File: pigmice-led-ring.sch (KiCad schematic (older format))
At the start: 27 parts, among them J1 Conn_01x02_Female, J2 Conn_01x03_Female

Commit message: WIP v0.3.0 work
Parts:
- removed D1, D10, D11, D12, D13, D14, D15, D16, D17, D18, D19, D2, D20, D21, D22, D23, D24, D3, D4, D5, D6, D7, D8, D9: LED, LED_SMD:LED_Avago_PLCC4_3.2x2.8mm_CW, symbol Device:LED
- removed PS1: RCD-24-0.35_Vref, CONV_RCD-24-0:Vref, symbol RCD-24-0.35_Vref:RCD-24-0.35_Vref
- added C1: 2.2uF, Capacitor_SMD:C_0805_2012Metric, symbol Device:C
- added C2: 4.7uF, Capacitor_SMD:C_0805_2012Metric, symbol Device:C
- added CF1: 330pF, Capacitor_SMD:C_0805_2012Metric, symbol Device:C
- added D1: D_Schottky, Diode_SMD:D_SOD-123, symbol Device:D_Schottky
- added D10, D11, D12, D13, D14, D15, D16, D17, D18, D19, D2, D20, D21, D22, D23, D24, D25, D26, D3, D4, D5, D6, D7, D8, D9: LED, led-ring:LED_Avago_PLCC4_3.2x2.8mm_CW, symbol Device:LED_Small
- added L1: 10uH, Inductor_SMD:L_Taiyo-Yuden_NR-40xx, symbol Device:L
- added R1: 203k, Resistor_SMD:R_0805_2012Metric, symbol Device:R
- added R2: 13.3k, Resistor_SMD:R_0805_2012Metric, symbol Device:R
- added R3: 47k, Resistor_SMD:R_0805_2012Metric, symbol Device:R_Small
- added R4, R5, R6, R7, R8: 150Ω, Resistor_SMD:R_0805_2012Metric, symbol Device:R_Small
- added U1: LMR62014XMF, Package_TO_SOT_SMD:SOT-23-5, symbol Regulator_Switching:LMR62014XMF
- J1: footprint led-ring:45A-VERT-PAIR -> Connector_Wire:SolderWirePad_1x02_P3.81mm_Drill1mm
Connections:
- net labels added: Vbat, Vled
- net labels removed: NULL, VCC
- wire segments 61 -> 59
- no-connect marks 2 -> 1
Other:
- note added: "20V output"

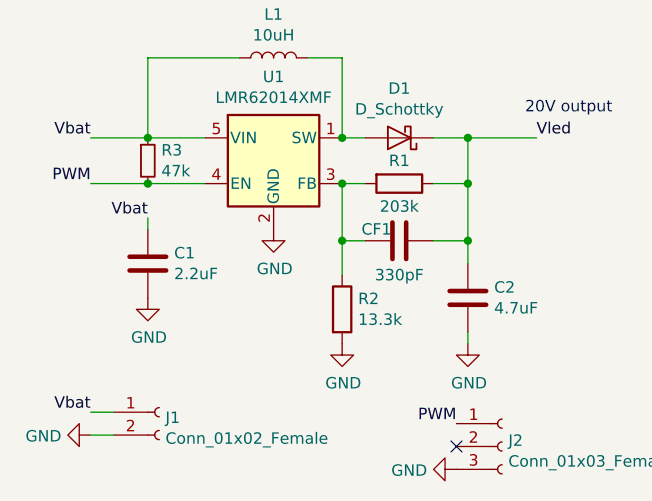
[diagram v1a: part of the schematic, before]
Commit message: Fix R2/CF1 labels
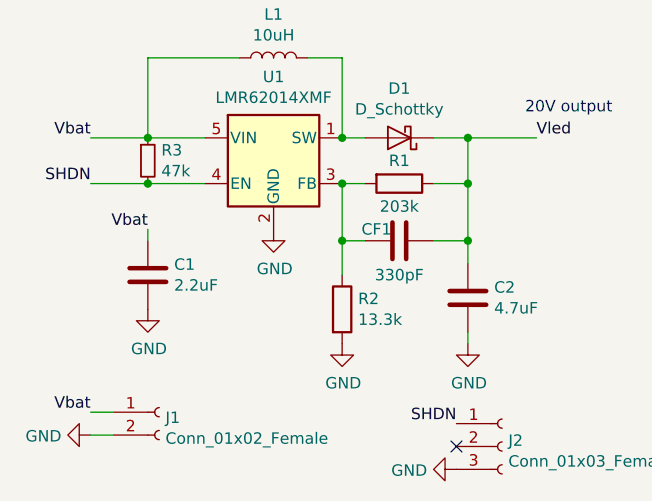
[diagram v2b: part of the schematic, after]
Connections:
- net PWM renamed SHDN
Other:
- moved on the sheet: C1
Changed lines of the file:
@@
 Vbat
 Text Label 1650 3450 2    50   ~ 0
-PWM
+SHDN
 $Comp
 L Device:D_Schottky D1
@@
 	0    -1   -1   0
 $EndComp
-$Comp
-L Device:C C2
-U 1 1 5E1D29D8
-P 3300 3950
-F 0 "C2" H 3415 3996 50  0000 L CNN
-F 1 "4.7uF" H 3415 3905 50  0000 L CNN
-F 2 "Capacitor_SMD:C_0805_2012Metric" H 3338 3800 50  0001 C CNN
-F 3 "~" H 3300 3950 50  0001 C CNN
-	1    3300 3950
-	1    0    0    -1
-$EndComp
 Text Label 3600 3250 0    50   ~ 0
 Vled
@@
 Connection ~ 2750 3700
 Wire Wire Line
-	3300 4150 3300 4100
-Wire Wire Line
 	3150 3700 3300 3700
 Wire Wire Line
-	3300 3700 3300 3800
-Wire Wire Line
 	3150 3450 3300 3450
 Wire Wire Line
 	3300 3450 3300 3700
-Connection ~ 3300 3700
 Wire Wire Line
 	3150 3250 3300 3250
@@
 $EndComp
 Text Label 3250 4500 2    50   ~ 0
-PWM
+SHDN
 NoConn ~ 3250 4600
 Wire Wire Line
@@
 	1650 3250 1900 3250
 Connection ~ 1900 3250
-Wire Wire Line
-	2150 3250 1900 3250
 Wire Wire Line
 	1900 2900 1900 3250
@@
 	4700 4500 4550 4500
 Connection ~ 4700 4500
-Wire Wire Line
-	1650 3450 1900 3450
-Text Label 1900 3600 2    50   ~ 0
+Text Label 1900 3650 2    50   ~ 0
 Vbat
 Wire Wire Line
-	1900 3600 1900 3650
+	1900 3650 1900 3700
 $Comp
 L Device:C C1
 U 1 1 5E1D1330
-P 1900 3800
-F 0 "C1" H 2015 3846 50  0000 L CNN
-F 1 "2.2uF" H 2015 3755 50  0000 L CNN
-F 2 "Capacitor_SMD:C_0805_2012Metric" H 1938 3650 50  0001 C CNN
-F 3 "~" H 1900 3800 50  0001 C CNN
-	1    1900 3800
+P 1900 3850
+F 0 "C1" H 2015 3896 50  0000 L CNN
+F 1 "2.2uF" H 2015 3805 50  0000 L CNN
+F 2 "Capacitor_SMD:C_0805_2012Metric" H 1938 3700 50  0001 C CNN
+F 3 "~" H 1900 3850 50  0001 C CNN
+	1    1900 3850
 	1    0    0    -1
 $EndComp
@@
 L power:GND #PWR0101
 U 1 1 5E24B903
-P 1900 3950
-F 0 "#PWR0101" H 1900 3700 50  0001 C CNN
-F 1 "GND" H 1905 3777 50  0000 C CNN
-F 2 "" H 1900 3950 50  0001 C CNN
-F 3 "" H 1900 3950 50  0001 C CNN
-	1    1900 3950
+P 1900 4000
+F 0 "#PWR0101" H 1900 3750 50  0001 C CNN
+F 1 "GND" H 1905 3827 50  0000 C CNN
+F 2 "" H 1900 4000 50  0001 C CNN
+F 3 "" H 1900 4000 50  0001 C CNN
+	1    1900 4000
 	1    0    0    -1
 $EndComp
@@
 $EndComp
 $Comp
+L Device:R_Small R8
+U 1 1 5E1D7BE7
+P 5900 3150
+F 0 "R8" H 5959 3196 50  0000 L CNN
+F 1 "150Ω" H 5959 3105 50  0000 L CNN
+F 2 "Resistor_SMD:R_0805_2012Metric" H 5900 3150 50  0001 C CNN
+F 3 "~" H 5900 3150 50  0001 C CNN
+	1    5900 3150
+	1    0    0    -1
+$EndComp
+$Comp
+L Device:LED_Small D22
+U 1 1 5E1D7BEE
+P 5900 3400
+F 0 "D22" V 5946 3332 50  0000 R CNN
+F 1 "LED" V 5855 3332 50  0000 R CNN
+F 2 "led-ring:LED_Avago_PLCC4_3.2x2.8mm_CW" V 5900 3400 50  0001 C CNN
+F 3 "~" V 5900 3400 50  0001 C CNN
+	1    5900 3400
+	0    -1   -1   0
+$EndComp
+$Comp
+L Device:LED_Small D23
+U 1 1 5E1D7BF5
+P 5900 3650
+F 0 "D23" V 5946 3582 50  0000 R CNN
+F 1 "LED" V 5855 3582 50  0000 R CNN
+F 2 "led-ring:LED_Avago_PLCC4_3.2x2.8mm_CW" V 5900 3650 50  0001 C CNN
+F 3 "~" V 5900 3650 50  0001 C CNN
+	1    5900 3650
+	0    -1   -1   0
+$EndComp
+$Comp
+L Device:LED_Small D24
+U 1 1 5E1D7BFC
+P 5900 3900
+F 0 "D24" V 5946 3832 50  0000 R CNN
+F 1 "LED" V 5855 3832 50  0000 R CNN
+F 2 "led-ring:LED_Avago_PLCC4_3.2x2.8mm_CW" V 5900 3900 50  0001 C CNN
+F 3 "~" V 5900 3900 50  0001 C CNN
+	1    5900 3900
+	0    -1   -1   0
+$EndComp
+$Comp
+L Device:LED_Small D25
+U 1 1 5E1D7C03
+P 5900 4150
+F 0 "D25" V 5946 4082 50  0000 R CNN
+F 1 "LED" V 5855 4082 50  0000 R CNN
+F 2 "led-ring:LED_Avago_PLCC4_3.2x2.8mm_CW" V 5900 4150 50  0001 C CNN
+F 3 "~" V 5900 4150 50  0001 C CNN
+	1    5900 4150
+	0    -1   -1   0
+$EndComp
+$Comp
+L Device:LED_Small D26
+U 1 1 5E1D7C0A
+P 5900 4400
+F 0 "D26" V 5946 4332 50  0000 R CNN
+F 1 "LED" V 5855 4332 50  0000 R CNN
+F 2 "led-ring:LED_Avago_PLCC4_3.2x2.8mm_CW" V 5900 4400 50  0001 C CNN
+F 3 "~" V 5900 4400 50  0001 C CNN
+	1    5900 4400
+	0    -1   -1   0
+$EndComp
+Wire Wire Line
+	5900 3250 5900 3300
+Wire Wire Line
+	5900 3550 5900 3500
+Wire Wire Line
+	5900 3750 5900 3800
+Wire Wire Line
+	5900 4000 5900 4050
+Wire Wire Line
+	5900 4250 5900 4300
+Wire Wire Line
+	5600 3050 5900 3050
+Connection ~ 5600 3050
+Wire Wire Line
+	5900 4500 5600 4500
+Connection ~ 5600 4500
+Connection ~ 3300 3700
+Wire Wire Line
+	3300 3700 3300 3800
+$Comp
 L power:GND #PWR0107
 U 1 1 5E254103
@@
 	1    0    0    -1
 $EndComp
+Wire Wire Line
+	3300 4150 3300 4100
+$Comp
+L Device:C C2
+U 1 1 5E1D29D8
+P 3300 3950
+F 0 "C2" H 3415 3996 50  0000 L CNN
+F 1 "4.7uF" H 3415 3905 50  0000 L CNN
+F 2 "Capacitor_SMD:C_0805_2012Metric" H 3338 3800 50  0001 C CNN
+F 3 "~" H 3300 3950 50  0001 C CNN
+	1    3300 3950
+	1    0    0    -1
+$EndComp
+Connection ~ 1900 3450
+Wire Wire Line
+	1650 3450 1900 3450
+Wire Wire Line
+	1900 3450 2150 3450
+Wire Wire Line
+	2150 3250 1900 3250
 $Comp
 L Device:R_Small R3
@@
 	1    0    0    -1
 $EndComp
-Connection ~ 1900 3450
-Wire Wire Line
-	1900 3450 2150 3450
-$Comp
-L Device:R_Small R8
-U 1 1 5E1D7BE7
-P 5900 3150
-F 0 "R8" H 5959 3196 50  0000 L CNN
-F 1 "150Ω" H 5959 3105 50  0000 L CNN
-F 2 "Resistor_SMD:R_0805_2012Metric" H 5900 3150 50  0001 C CNN
-F 3 "~" H 5900 3150 50  0001 C CNN
-	1    5900 3150
-	1    0    0    -1
-$EndComp
-$Comp
-L Device:LED_Small D22
-U 1 1 5E1D7BEE
-P 5900 3400
-F 0 "D22" V 5946 3332 50  0000 R CNN
-F 1 "LED" V 5855 3332 50  0000 R CNN
-F 2 "led-ring:LED_Avago_PLCC4_3.2x2.8mm_CW" V 5900 3400 50  0001 C CNN
-F 3 "~" V 5900 3400 50  0001 C CNN
-	1    5900 3400
-	0    -1   -1   0
-$EndComp
-$Comp
-L Device:LED_Small D23
-U 1 1 5E1D7BF5
-P 5900 3650
-F 0 "D23" V 5946 3582 50  0000 R CNN
-F 1 "LED" V 5855 3582 50  0000 R CNN
-F 2 "led-ring:LED_Avago_PLCC4_3.2x2.8mm_CW" V 5900 3650 50  0001 C CNN
-F 3 "~" V 5900 3650 50  0001 C CNN
-	1    5900 3650
-	0    -1   -1   0
-$EndComp
-$Comp
-L Device:LED_Small D24
-U 1 1 5E1D7BFC
-P 5900 3900
-F 0 "D24" V 5946 3832 50  0000 R CNN
-F 1 "LED" V 5855 3832 50  0000 R CNN
-F 2 "led-ring:LED_Avago_PLCC4_3.2x2.8mm_CW" V 5900 3900 50  0001 C CNN
-F 3 "~" V 5900 3900 50  0001 C CNN
-	1    5900 3900
-	0    -1   -1   0
-$EndComp
-$Comp
-L Device:LED_Small D25
-U 1 1 5E1D7C03
-P 5900 4150
-F 0 "D25" V 5946 4082 50  0000 R CNN
-F 1 "LED" V 5855 4082 50  0000 R CNN
-F 2 "led-ring:LED_Avago_PLCC4_3.2x2.8mm_CW" V 5900 4150 50  0001 C CNN
-F 3 "~" V 5900 4150 50  0001 C CNN
-	1    5900 4150
-	0    -1   -1   0
-$EndComp
-$Comp
-L Device:LED_Small D26
-U 1 1 5E1D7C0A
-P 5900 4400
-F 0 "D26" V 5946 4332 50  0000 R CNN
-F 1 "LED" V 5855 4332 50  0000 R CNN
-F 2 "led-ring:LED_Avago_PLCC4_3.2x2.8mm_CW" V 5900 4400 50  0001 C CNN
-F 3 "~" V 5900 4400 50  0001 C CNN
-	1    5900 4400
-	0    -1   -1   0
-$EndComp
-Wire Wire Line
-	5900 3250 5900 3300
-Wire Wire Line
-	5900 3550 5900 3500
-Wire Wire Line
-	5900 3750 5900 3800
-Wire Wire Line
-	5900 4000 5900 4050
-Wire Wire Line
-	5900 4250 5900 4300
-Wire Wire Line
-	5600 3050 5900 3050
-Connection ~ 5600 3050
-Wire Wire Line
-	5900 4500 5600 4500
-Connection ~ 5600 4500
 $EndSCHEMATC

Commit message: Swap out inductor for smaller 2410 footprint
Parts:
- L1: footprint Inductor_SMD:L_Taiyo-Yuden_NR-40xx -> Inductor_SMD:L_Taiyo-Yuden_NR-24xx
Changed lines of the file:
@@
 F 0 "L1" V 2640 2900 50  0000 C CNN
 F 1 "10uH" V 2549 2900 50  0000 C CNN
-F 2 "Inductor_SMD:L_Taiyo-Yuden_NR-40xx" H 2450 2900 50  0001 C CNN
+F 2 "Inductor_SMD:L_Taiyo-Yuden_NR-24xx" H 2450 2900 50  0001 C CNN
 F 3 "~" H 2450 2900 50  0001 C CNN
 	1    2450 2900

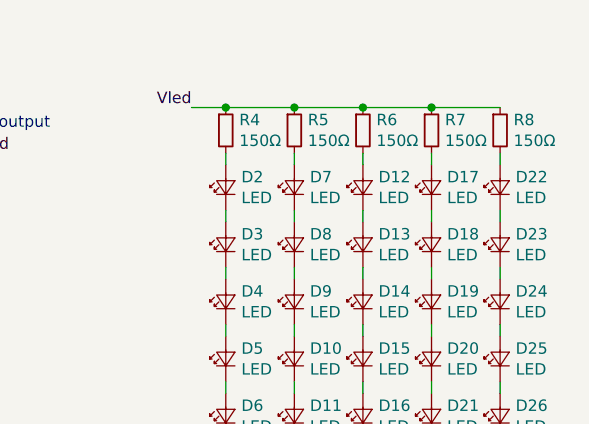
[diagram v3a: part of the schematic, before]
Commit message: Switch from 150 to 137 ohm resistors for LEDs
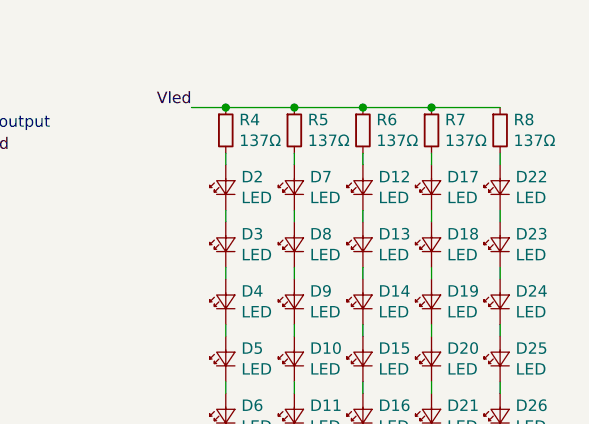
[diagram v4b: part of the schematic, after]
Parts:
- R4, R5, R6, R7, R8: value 150Ω -> 137Ω
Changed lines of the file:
@@
 P 4700 3150
 F 0 "R4" H 4759 3196 50  0000 L CNN
-F 1 "150Ω" H 4759 3105 50  0000 L CNN
+F 1 "137Ω" H 4759 3105 50  0000 L CNN
 F 2 "Resistor_SMD:R_0805_2012Metric" H 4700 3150 50  0001 C CNN
 F 3 "~" H 4700 3150 50  0001 C CNN
@@
 P 5000 3150
 F 0 "R5" H 5059 3196 50  0000 L CNN
-F 1 "150Ω" H 5059 3105 50  0000 L CNN
+F 1 "137Ω" H 5059 3105 50  0000 L CNN
 F 2 "Resistor_SMD:R_0805_2012Metric" H 5000 3150 50  0001 C CNN
 F 3 "~" H 5000 3150 50  0001 C CNN
@@
 P 5300 3150
 F 0 "R6" H 5359 3196 50  0000 L CNN
-F 1 "150Ω" H 5359 3105 50  0000 L CNN
+F 1 "137Ω" H 5359 3105 50  0000 L CNN
 F 2 "Resistor_SMD:R_0805_2012Metric" H 5300 3150 50  0001 C CNN
 F 3 "~" H 5300 3150 50  0001 C CNN
@@
 P 5600 3150
 F 0 "R7" H 5659 3196 50  0000 L CNN
-F 1 "150Ω" H 5659 3105 50  0000 L CNN
+F 1 "137Ω" H 5659 3105 50  0000 L CNN
 F 2 "Resistor_SMD:R_0805_2012Metric" H 5600 3150 50  0001 C CNN
 F 3 "~" H 5600 3150 50  0001 C CNN
@@
 P 5900 3150
 F 0 "R8" H 5959 3196 50  0000 L CNN
-F 1 "150Ω" H 5959 3105 50  0000 L CNN
+F 1 "137Ω" H 5959 3105 50  0000 L CNN
 F 2 "Resistor_SMD:R_0805_2012Metric" H 5900 3150 50  0001 C CNN
 F 3 "~" H 5900 3150 50  0001 C CNN

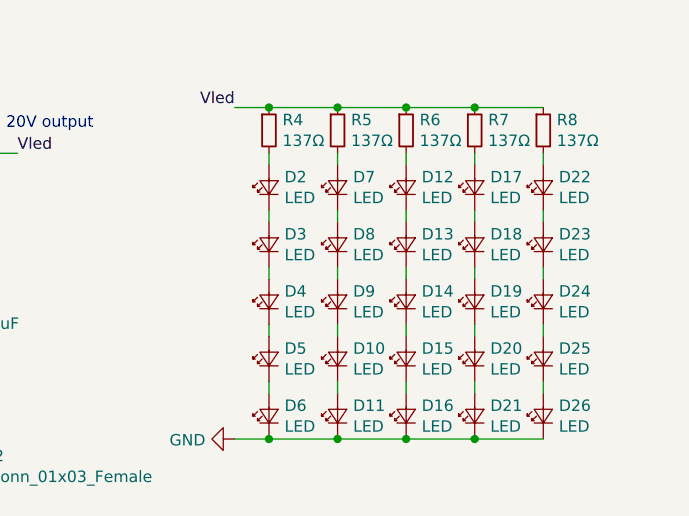
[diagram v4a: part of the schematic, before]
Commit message: Use CCRs instead of resistors
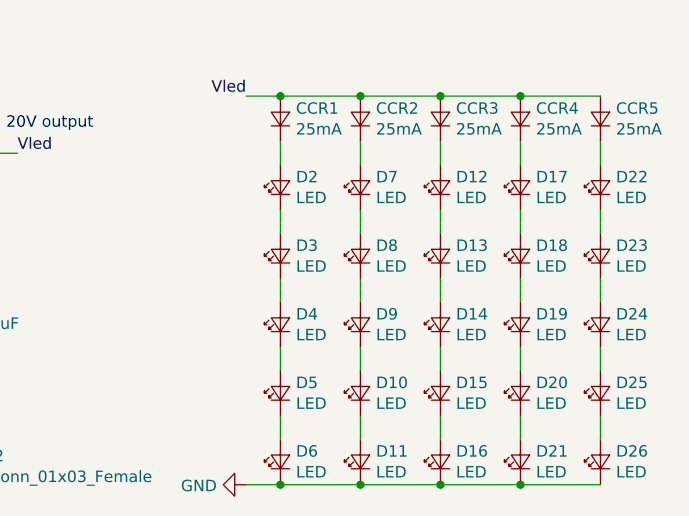
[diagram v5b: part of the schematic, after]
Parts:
- removed R4, R5, R6, R7, R8: 137Ω, Resistor_SMD:R_0805_2012Metric, symbol Device:R_Small
- added CCR1, CCR2, CCR3, CCR4, CCR5: 25mA, Diode_SMD:D_SOD-123, symbol Device:D_Small
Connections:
- net Vled: now also CCR1.2 (A), CCR2.2 (A), CCR3.2 (A), CCR4.2 (A), CCR5.2 (A)
- net at D22.2 (A): now also CCR5.1 (K)
- net at D2.2 (A): now also CCR1.1 (K)
- net at D7.2 (A): now also CCR2.1 (K)
- net at D12.2 (A): now also CCR3.1 (K)
- net at D17.2 (A): now also CCR4.1 (K)

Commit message: Add mini badge
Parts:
- added BT1: Battery_Cell, Battery:BatteryHolder_LINX_BAT-HLD-012-SMT, symbol Device:Battery_Cell
- added D27, D28, D29, D30: LED, LED_SMD:LED_0603_1608Metric, symbol Device:LED
- added R4, R5: 47Ω, Resistor_SMD:R_0603_1608Metric, symbol Device:R
- added R6, R7: 56Ω, Resistor_SMD:R_0603_1608Metric, symbol Device:R
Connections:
- new net: BT1.1 (+), R4.1, R5.1, R6.1, R7.1
- new net: BT1.2 (-), D27.1 (K), D28.1 (K), D29.1 (K), D30.1 (K)
- new net: D27.2 (A), R4.2
- new net: D28.2 (A), R5.2
- new net: D29.2 (A), R6.2
- new net: D30.2 (A), R7.2
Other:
- note added: "Badge"
- note added: "LED Array"
- note added: "Voltage Regulator"
- moved on the sheet: C1, C2, CCR1, CCR2, CCR3, CCR4, CCR5, CF1, D1, D10, D11, D12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

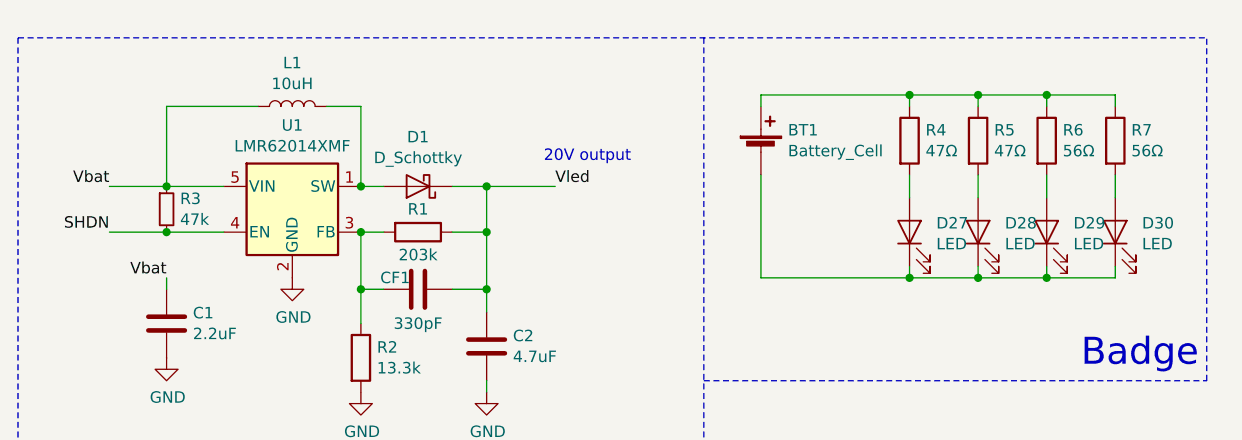
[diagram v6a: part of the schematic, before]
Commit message: Add button to mini-badge
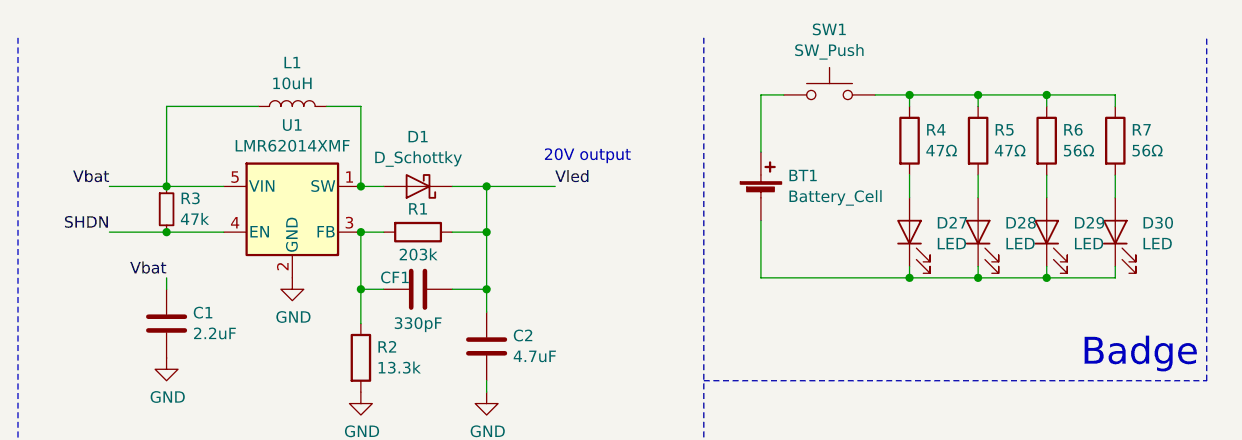
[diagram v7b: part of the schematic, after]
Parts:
- added SW1: SW_Push, Button_Switch_SMD:SW_SPST_B3U-1100P, symbol Switch:SW_Push
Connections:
- net at R4.1, R5.1, R6.1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: now also SW1.2; no longer BT1.1 (+)
- new net: BT1.1 (+), SW1.1
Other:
- moved on the sheet: BT1
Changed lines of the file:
@@
 L Device:Battery_Cell BT1
 U 1 1 5E2E9E0D
-P 3750 1000
-F 0 "BT1" H 3868 1096 50  0000 L CNN
-F 1 "Battery_Cell" H 3868 1005 50  0000 L CNN
-F 2 "Battery:BatteryHolder_LINX_BAT-HLD-012-SMT" V 3750 1060 50  0001 C CNN
-F 3 "~" V 3750 1060 50  0001 C CNN
-	1    3750 1000
+P 3750 1200
+F 0 "BT1" H 3868 1296 50  0000 L CNN
+F 1 "Battery_Cell" H 3868 1205 50  0000 L CNN
+F 2 "Battery:BatteryHolder_LINX_BAT-HLD-012-SMT" V 3750 1260 50  0001 C CNN
+F 3 "~" V 3750 1260 50  0001 C CNN
+	1    3750 1200
 	1    0    0    -1
 $EndComp
@@
 Wire Notes Line
 	5700 2000 5700 500
-Wire Notes Line
-	500  500  5700 500
 Text Notes 5150 1950 0    118  ~ 0
 Badge
-Wire Wire Line
-	3750 800  3750 750
-Wire Wire Line
-	3750 750  4400 750
 Wire Wire Line
 	4400 750  4400 800
@@
 Wire Wire Line
 	4700 750  4700 800
-Connection ~ 4400 750
 Wire Wire Line
 	4700 750  5000 750
@@
 	4400 1550 4400 1500
 Wire Wire Line
-	3750 1100 3750 1550
-Wire Wire Line
 	4400 1550 4700 1550
 Wire Wire Line
@@
 	5300 1550 5300 1500
 Connection ~ 5000 1550
+$Comp
+L Switch:SW_Push SW1
+U 1 1 5E2C1562
+P 4050 750
+F 0 "SW1" H 4050 1035 50  0000 C CNN
+F 1 "SW_Push" H 4050 944 50  0000 C CNN
+F 2 "Button_Switch_SMD:SW_SPST_B3U-1100P" H 4050 950 50  0001 C CNN
+F 3 "~" H 4050 950 50  0001 C CNN
+	1    4050 750
+	1    0    0    -1
+$EndComp
+Wire Wire Line
+	3750 1550 3750 1300
+Wire Wire Line
+	3750 750  3850 750
+Wire Wire Line
+	3750 750  3750 1000
+Wire Wire Line
+	4250 750  4400 750
+Connection ~ 4400 750
 $EndSCHEMATC
